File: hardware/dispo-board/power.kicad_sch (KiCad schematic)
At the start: 23 parts, among them U1 TPS79633DCQ, U8 TLV75710PDBV

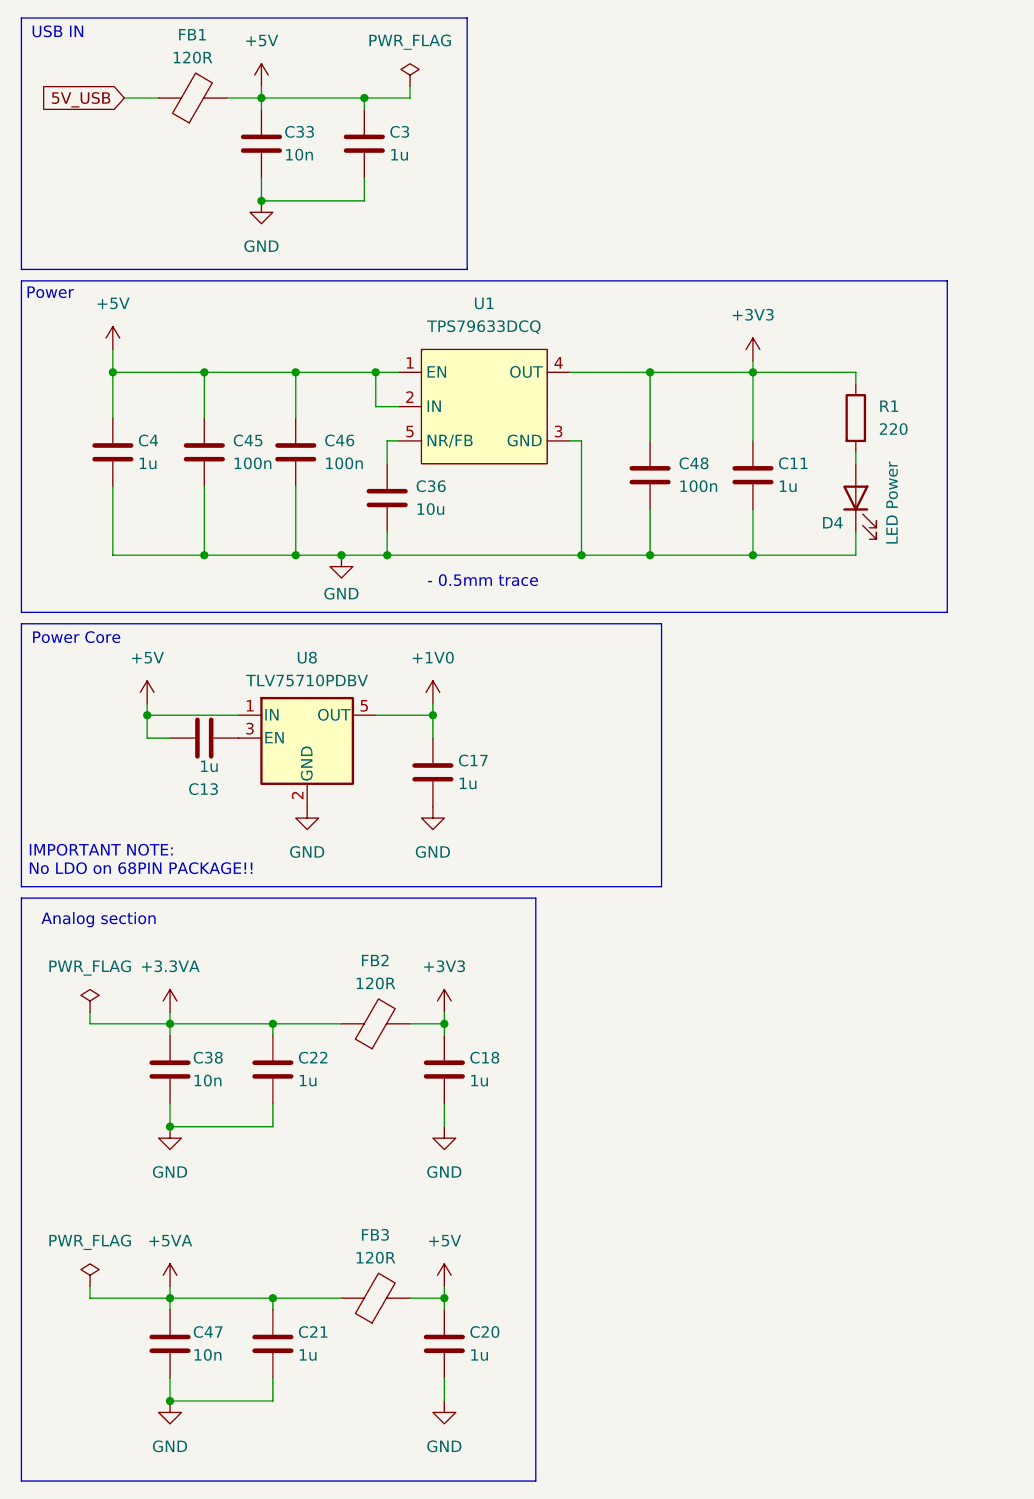
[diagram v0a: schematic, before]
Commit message: deleted nucleo board files, schematic ready?, changed to usb c
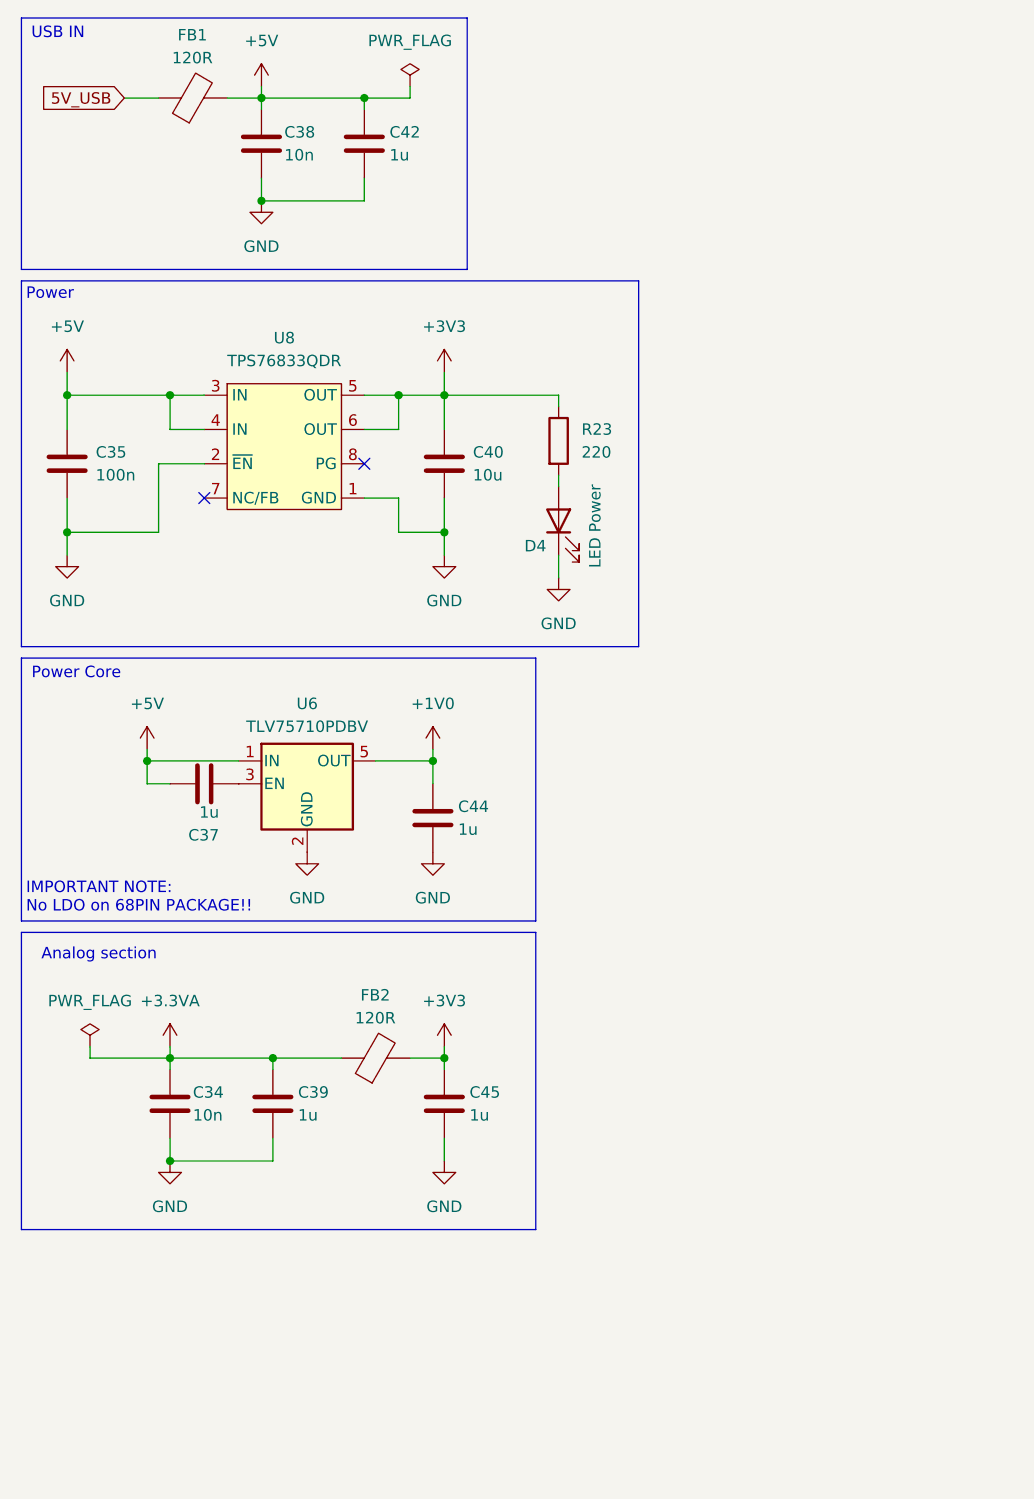
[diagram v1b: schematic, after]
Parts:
- removed C11, C20, C21, C4: 1u, Capacitor_SMD:C_0402_1005Metric, symbol Device:C
- removed C36: 10u, Capacitor_SMD:C_0603_1608Metric, symbol Device:C
- removed C45, C46, C48: 100n, Capacitor_SMD:C_0402_1005Metric, symbol Device:C
- removed C47: 10n, Capacitor_SMD:C_0402_1005Metric, symbol Device:C
- removed FB3: 120R, Resistor_SMD:R_0402_1005Metric, symbol Device:FerriteBead
- removed R1: 220, symbol Device:R
- removed U1: TPS79633DCQ, Package_TO_SOT_SMD:SOT-223-6, symbol MySymbols:TPS79633DCQ
- added C35: 100n, Capacitor_SMD:C_0402_1005Metric, symbol Device:C
- added C40: 10u, Capacitor_SMD:C_0603_1608Metric, symbol Device:C
- added R23: 220, Resistor_SMD:R_0402_1005Metric, symbol Device:R
- added U8: TPS76833QDR, Package_SO:SOIC-8-1EP_3.9x4.9mm_P1.27mm_EP2.95x4.9mm_Mask2.71x3.4mm, symbol MySymbols:SPX3940T-L-3-3/TR
- renumbered C38 to C34, C13 to C37, C33 to C38, C22 to C39, C3 to C42, C17 to C44, C18 to C45, U8 to U6
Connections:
- net +3V3: now also C40.1, R23.1, U8.5 (OUT), U8.6 (OUT)
- net +5V: now also C35.1, U8.3 (IN), U8.4 (IN)
- net GND: now also C35.2, C40.2, U8.1 (GND), U8.2 (~{EN})
- net at D4.2 (A): now also R23.2
- no-connect marks 0 -> 2
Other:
- note removed: "- 0.5mm trace"
- moved on the sheet: C34, C37, C39, C44, C45, FB2, U6

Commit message: changed to old ldo
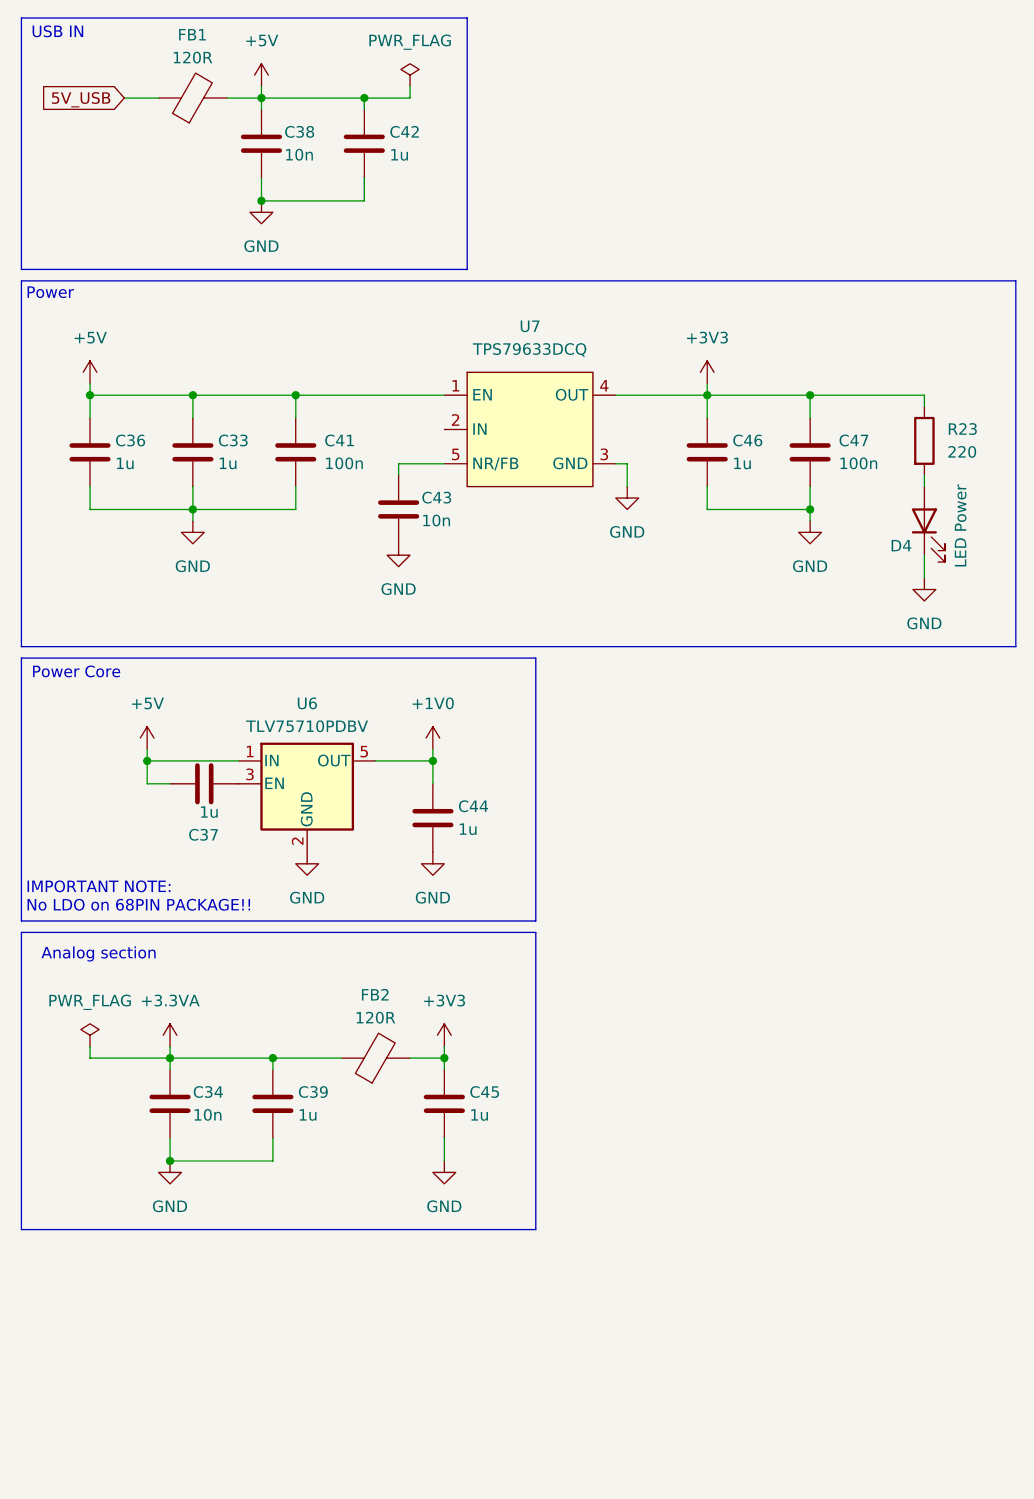
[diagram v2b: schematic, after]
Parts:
- removed C35: 100n, Capacitor_SMD:C_0402_1005Metric, symbol Device:C
- removed C40: 10u, Capacitor_SMD:C_0603_1608Metric, symbol Device:C
- removed U8: TPS76833QDR, Package_SO:SOIC-8-1EP_3.9x4.9mm_P1.27mm_EP2.95x4.9mm_Mask2.71x3.4mm, symbol MySymbols:SPX3940T-L-3-3/TR
- added C33, C36, C46: 1u, Capacitor_SMD:C_0402_1005Metric, symbol Device:C
- added C41, C47: 100n, Capacitor_SMD:C_0402_1005Metric, symbol Device:C
- added C43: 10n, Capacitor_SMD:C_0402_1005Metric, symbol Device:C
- added U7: TPS79633DCQ, Package_TO_SOT_SMD:SOT-223-6, symbol MySymbols:TPS79633DCQ
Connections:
- net +3V3: now also C46.1, C47.1, U7.4 (OUT)
- net +5V: now also C33.1, C36.1, C41.1, U7.1 (EN)
- net GND: now also C33.2, C36.2, C41.2, C43.2, C46.2, C47.2, U7.3 (GND), U7.6 (GND)
- new net: C43.1, U7.5 (NR/FB)
- no-connect marks 2 -> 0
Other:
- moved on the sheet: D4, R23

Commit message: corrected ldo schematic
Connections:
- net +5V: now also U7.2 (IN)
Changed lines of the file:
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@@
+	)
+	(junction
+		(at 59.69 55.88)
+		(diameter 0)
+		(color 0 0 0 0)
 	)
 	(junction
@@
 	(wire
 		(pts
-			(xy 45.72 55.88) (xy 62.23 55.88)
+			(xy 45.72 55.88) (xy 59.69 55.88)
 		)
 		(stroke
@@
 	(wire
 		(pts
+			(xy 59.69 59.69) (xy 59.69 55.88)
+		)
+		(stroke
+			(width 0)
+			(type default)
+		)
+	)
+	(wire
+		(pts
 			(xy 45.72 55.88) (xy 45.72 58.42)
 		)
@@
 	(wire
 		(pts
+			(xy 62.23 59.69) (xy 59.69 59.69)
+		)
+		(stroke
+			(width 0)
+			(type default)
+		)
+	)
+	(wire
+		(pts
 			(xy 45.72 68.58) (xy 45.72 66.04)
 		)
@@
 		)
 		(stroke
+			(width 0)
+			(type default)
+		)
+	)
+	(wire
+		(pts
+			(xy 59.69 55.88) (xy 62.23 55.88)
+		)
+		(stroke

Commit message: annotate schmetic
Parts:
- renumbered C36 to C33, C33 to C35, C37 to C36, C38 to C37, C39 to C38, C41 to C39, C42 to C40, C43 to C41, C44 to C42, C45 to C43, C46 to C44, C47 to C45, D4 to D3, R23 to R22

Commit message: shorted board
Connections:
- net +5V: now also C36.1, U6.3 (EN); no longer C36.2
- net GND: now also C36.2
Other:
- moved on the sheet: C36
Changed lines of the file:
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@@
 	(text "IMPORTANT NOTE:\nNo LDO on 68PIN PACKAGE!!"
 		(exclude_from_sim no)
-		(at 15.748 113.538 0)
+		(at 73.152 112.776 0)
 		(effects
 			(font
@@
 	)
 	(junction
-		(at 29.21 96.52)
+		(at 38.1 96.52)
 		(diameter 0)
 		(color 0 0 0 0)
@@
 	)
 	(junction
+		(at 30.48 96.52)
+		(diameter 0)
+		(color 0 0 0 0)
+	)
+	(junction
 		(at 22.86 55.88)
 		(diameter 0)
@@
 	(wire
 		(pts
-			(xy 29.21 96.52) (xy 39.37 96.52)
-		)
-		(stroke
-			(width 0)
-			(type default)
-		)
-	)
-	(wire
-		(pts
 			(xy 115.57 73.66) (xy 115.57 76.2)
 		)
@@
 	(wire
 		(pts
-			(xy 29.21 95.25) (xy 29.21 96.52)
+			(xy 30.48 95.25) (xy 30.48 96.52)
 		)
 		(stroke
@@
 	(wire
 		(pts
-			(xy 31.75 99.06) (xy 29.21 99.06)
+			(xy 102.87 55.88) (xy 102.87 58.42)
 		)
 		(stroke
@@
 	(wire
 		(pts
-			(xy 102.87 55.88) (xy 102.87 58.42)
+			(xy 81.28 63.5) (xy 82.55 63.5)
 		)
 		(stroke
@@
 	(wire
 		(pts
-			(xy 29.21 99.06) (xy 29.21 96.52)
+			(xy 59.69 59.69) (xy 59.69 55.88)
 		)
 		(stroke
@@
 	(wire
 		(pts
-			(xy 81.28 63.5) (xy 82.55 63.5)
+			(xy 45.72 55.88) (xy 45.72 58.42)
 		)
 		(stroke
@@
 	(wire
 		(pts
-			(xy 59.69 59.69) (xy 59.69 55.88)
+			(xy 62.23 59.69) (xy 59.69 59.69)
 		)
 		(stroke
@@
 	(wire
 		(pts
-			(xy 45.72 55.88) (xy 45.72 58.42)
+			(xy 45.72 68.58) (xy 45.72 66.04)
 		)
 		(stroke
@@
 	(wire
 		(pts
-			(xy 62.23 59.69) (xy 59.69 59.69)
+			(xy 57.15 63.5) (xy 57.15 64.77)
 		)
 		(stroke
@@
 	(wire
 		(pts
-			(xy 45.72 68.58) (xy 45.72 66.04)
+			(xy 22.86 68.58) (xy 34.29 68.58)
 		)
 		(stroke
@@
 	(wire
 		(pts
-			(xy 57.15 63.5) (xy 57.15 64.77)
+			(xy 31.75 128.27) (xy 31.75 129.54)
 		)
 		(stroke
@@
 	(wire
 		(pts
-			(xy 22.86 68.58) (xy 34.29 68.58)
+			(xy 31.75 129.54) (xy 31.75 130.81)
 		)
 		(stroke
@@
 	(wire
 		(pts
-			(xy 31.75 128.27) (xy 31.75 129.54)
+			(xy 39.37 99.06) (xy 38.1 99.06)
 		)
 		(stroke
@@
 	(wire
 		(pts
-			(xy 31.75 129.54) (xy 31.75 130.81)
+			(xy 53.34 22.86) (xy 58.42 22.86)
 		)
 		(stroke
@@
 	(wire
 		(pts
-			(xy 53.34 22.86) (xy 58.42 22.86)
+			(xy 91.44 66.04) (xy 91.44 68.58)
 		)
 		(stroke
@@
 	(wire
 		(pts
-			(xy 91.44 66.04) (xy 91.44 68.58)
+			(xy 91.44 68.58) (xy 102.87 68.58)
 		)
 		(stroke
@@
 	(wire
 		(pts
-			(xy 91.44 68.58) (xy 102.87 68.58)
+			(xy 34.29 66.04) (xy 34.29 68.58)
 		)
 		(stroke
@@
 	(wire
 		(pts
-			(xy 34.29 66.04) (xy 34.29 68.58)
+			(xy 41.91 34.29) (xy 53.34 34.29)
 		)
 		(stroke
@@
 	(wire
 		(pts
-			(xy 41.91 34.29) (xy 53.34 34.29)
+			(xy 30.48 96.52) (xy 38.1 96.52)
 		)
 		(stroke
@@
 	(wire
 		(pts
+			(xy 30.48 96.52) (xy 30.48 97.79)
+		)
+		(stroke
+			(width 0)
+			(type default)
+		)
+	)
+	(wire
+		(pts
 			(xy 41.91 21.59) (xy 41.91 22.86)
 		)
@@
 	(wire
 		(pts
+			(xy 38.1 99.06) (xy 38.1 96.52)
+		)
+		(stroke
+			(width 0)
+			(type default)
+		)
+	)
+	(wire
+		(pts
 			(xy 53.34 31.75) (xy 53.34 34.29)
 		)
@@
 		)
 	)
+	(wire
+		(pts
+			(xy 38.1 96.52) (xy 39.37 96.52)
+		)
+		(stroke
+			(width 0)
+			(type default)
+		)
+	)
 	(global_label "5V_USB"
 		(shape input)
@@
 	)
 	(symbol
+		(lib_id "power:GND")
+		(at 30.48 105.41 0)
+		(unit 1)
+		(exclude_from_sim no)
+		(in_bom yes)
+		(on_board yes)
+		(dnp no)
+		(fields_autoplaced yes)
+		(property "Reference" "#PWR093"
+			(at 30.48 111.76 0)
+			(effects
+				(font
+					(size 1.27 1.27)
+				)
+				(hide yes)
+			)
+		)
+		(property "Value" "GND"
+			(at 30.48 110.49 0)
+			(effects
+				(font
+					(size 1.27 1.27)
+				)
+			)
+		)
+		(property "Footprint" ""
+			(at 30.48 105.41 0)
+			(effects
+				(font
+					(size 1.27 1.27)
+				)
+				(hide yes)
+			)
+		)
+		(property "Datasheet" ""
+			(at 30.48 105.41 0)
+			(effects
+				(font
+					(size 1.27 1.27)
+				)
+				(hide yes)
+			)
+		)
+		(property "Description" "Power symbol creates a global label with name \"GND\" , ground"
+			(at 30.48 105.41 0)
+			(effects
+				(font
+					(size 1.27 1.27)
+				)
+				(hide yes)
+			)
+		)
+		(pin "1"
+		)
+		(instances
+			(project "dispo-board"
+				(path "/93ea4da8-8485-4fb5-a89d-c72021d94c09/7d68ca4b-31d3-4e96-884d-dc968b70719c"
+					(reference "#PWR093")
+					(unit 1)
+				)
+			)
+		)
+	)
+	(symbol
 		(lib_id "power:PWR_FLAG")
 		(at 22.86 128.27 0)
@@
 	(symbol
 		(lib_id "Device:C")
-		(at 35.56 99.06 270)
+		(at 30.48 101.6 0)
 		(unit 1)
 		(exclude_from_sim no)
@@
 		(dnp no)
 		(property "Reference" "C36"
-			(at 37.211 104.775 90)
+			(at 36.83 100.33 0)
 			(effects
 				(font
@@
 		)
 		(property "Value" "1u"
-			(at 37.211 102.235 90)
+			(at 35.56 102.616 0)
 			(effects
 				(font
@@
 		)
 		(property "Footprint" "Capacitor_SMD:C_0402_1005Metric"
-			(at 31.75 100.0252 0)
+			(at 31.4452 105.41 0)
 			(effects
 				(font
@@
 		)
 		(property "Datasheet" "~"
-			(at 35.56 99.06 0)
+			(at 30.48 101.6 0)
 			(effects
 				(font
@@
 		)
 		(property "Description" "Unpolarized capacitor"
-			(at 35.56 99.06 0)
+			(at 30.48 101.6 0)
 			(effects
 				(font
@@
 		)
 		(property "MOUSER_NR" "963-LMK105BJ105MVHF"
-			(at 35.56 99.06 0)
+			(at 30.48 101.6 0)
 			(effects
 				(font
@@
 	(symbol
 		(lib_id "power:+5V")
-		(at 29.21 95.25 0)
+		(at 30.48 95.25 0)
 		(unit 1)
 		(exclude_from_sim no)
@@
 		(fields_autoplaced yes)
 		(property "Reference" "#PWR077"
-			(at 29.21 99.06 0)
+			(at 30.48 99.06 0)
 			(effects
 				(font
@@
 		)
 		(property "Value" "+5V"
-			(at 29.21 90.17 0)
+			(at 30.48 90.17 0)
 			(effects
 				(font
@@
 		)
 		(property "Footprint" ""
-			(at 29.21 95.25 0)
+			(at 30.48 95.25 0)
 			(effects
 				(font
@@
 		)
 		(property "Datasheet" ""
-			(at 29.21 95.25 0)
+			(at 30.48 95.25 0)
 			(effects
 				(font
@@
 		)
 		(property "Description" "Power symbol creates a global label with name \"+5V\""
-			(at 29.21 95.25 0)
+			(at 30.48 95.25 0)
 			(effects
 				(font

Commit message: ordered pcb and stuff
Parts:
- U6: MOUSER_NR (none) -> 595-TLV75710PDBVR
- U7: MOUSER_NO 595-TPS79633DCQ -> (none); MOUSER_NR (none) -> 595-TPS79633DCQ
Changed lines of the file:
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@@
+			)
+		)
+		(property "MOUSER_NO" ""
+			(at 62.23 134.62 0)
+			(effects
+				(font
+					(size 1.27 1.27)
+				)
+				(hide yes)
 			)
 		)
@@
 			)
 		)
+		(property "MOUSER_NO" ""
+			(at 57.15 68.58 0)
+			(effects
+				(font
+					(size 1.27 1.27)
+				)
+				(hide yes)
+			)
+		)
 		(pin "1"
 		)
@@
 		)
 		(property "MOUSER_NR" "963-LMK105BJ105MVHF"
+			(at 43.18 134.62 0)
+			(effects
+				(font
+					(size 1.27 1.27)
+				)
+				(hide yes)
+			)
+		)
+		(property "MOUSER_NO" ""
 			(at 43.18 134.62 0)
 			(effects
@@
 			)
 		)
+		(property "MOUSER_NO" ""
+			(at 34.29 22.86 90)
+			(effects
+				(font
+					(size 1.27 1.27)
+				)
+				(hide yes)
+			)
+		)
 		(pin "1"
 		)
@@
 		)
 		(property "MOUSER_NR" "963-LMK105BJ105MVHF"
+			(at 53.34 27.94 0)
+			(effects
+				(font
+					(size 1.27 1.27)
+				)
+				(hide yes)
+			)
+		)
+		(property "MOUSER_NO" ""
 			(at 53.34 27.94 0)
 			(effects
@@
 			)
 		)
+		(property "MOUSER_NO" ""
+			(at 54.61 129.54 90)
+			(effects
+				(font
+					(size 1.27 1.27)
+				)
+				(hide yes)
+			)
+		)
 		(pin "1"
 		)
@@
 			)
 		)
+		(property "MOUSER_NR" "595-TLV75710PDBVR"
+			(at 46.99 99.06 0)
+			(effects
+				(font
+					(size 1.27 1.27)
+				)
+				(hide yes)
+			)
+		)
+		(property "MOUSER_NO" ""
+			(at 46.99 99.06 0)
+			(effects
+				(font
+					(size 1.27 1.27)
+				)
+				(hide yes)
+			)
+		)
 		(pin "1"
 		)
@@
 			)
 		)
+		(property "MOUSER_NO" ""
+			(at 91.44 62.23 0)
+			(effects
+				(font
+					(size 1.27 1.27)
+				)
+				(hide yes)
+			)
+		)
 		(pin "2"
 		)
@@
 			)
 		)
+		(property "MOUSER_NO" ""
+			(at 115.57 60.96 0)
+			(effects
+				(font
+					(size 1.27 1.27)
+				)
+				(hide yes)
+			)
+		)
 		(pin "2"
 		)
@@
 			)
 		)
+		(property "MOUSER_NO" ""
+			(at 102.87 62.23 0)
+			(effects
+				(font
+					(size 1.27 1.27)
+				)
+				(hide yes)
+			)
+		)
 		(pin "2"
 		)
@@
 		)
 		(property "MOUSER_NR" "963-MCASL105SB7104KF"
+			(at 45.72 62.23 0)
+			(effects
+				(font
+					(size 1.27 1.27)
+				)
+				(hide yes)
+			)
+		)
+		(property "MOUSER_NO" ""
 			(at 45.72 62.23 0)
 			(effects
@@
 			)
 		)
+		(property "MOUSER_NO" ""
+			(at 41.91 27.94 0)
+			(effects
+				(font
+					(size 1.27 1.27)
+				)
+				(hide yes)
+			)
+		)
 		(pin "1"
 		)
@@
 			)
 		)
+		(property "MOUSER_NO" ""
+			(at 30.48 101.6 0)
+			(effects
+				(font
+					(size 1.27 1.27)
+				)
+				(hide yes)
+			)
+		)
 		(pin "2"
 		)
@@
 			)
 		)
+		(property "MOUSER_NO" ""
+			(at 22.86 62.23 0)
+			(effects
+				(font
+					(size 1.27 1.27)
+				)
+				(hide yes)
+			)
+		)
 		(pin "2"
 		)
@@
 		)
 		(property "MOUSER_NR" "963-LMK105BJ105MVHF"
+			(at 60.96 102.87 0)
+			(effects
+				(font
+					(size 1.27 1.27)
+				)
+				(hide yes)
+			)
+		)
+		(property "MOUSER_NO" ""
 			(at 60.96 102.87 0)
 			(effects
@@
 			)
 		)
-		(property "MOUSER_NO" "595-TPS79633DCQ"
+		(property "MOUSER_NR" "595-TPS79633DCQ"
+			(at 71.12 59.69 0)
+			(effects
+				(font
+					(size 1.27 1.27)
+				)
+				(hide yes)
+			)
+		)
+		(property "MOUSER_NO" ""
 			(at 71.12 59.69 0)
 			(effects
@@
 			)
 		)
+		(property "MOUSER_NO" ""
+			(at 34.29 62.23 0)
+			(effects
+				(font
+					(size 1.27 1.27)
+				)
+				(hide yes)
+			)
+		)
 		(pin "2"
 		)
@@
 			)
 		)
+		(property "MOUSER_NO" ""
+			(at 115.57 69.85 90)
+			(effects
+				(font
+					(size 1.27 1.27)
+				)
+				(hide yes)
+			)
+		)
 		(pin "2"
 		)
@@
 			(at 31.75 134.62 0)
 			(effects
+				(font
+					(size 1.27 1.27)
+				)
+				(hide yes)
+			)
+		)
+		(property "MOUSER_NO" ""
+			(at 31.75 134.62 0)
+			(effects
